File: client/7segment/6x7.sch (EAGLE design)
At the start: 26 parts, among them IC1 AT90S2313P, IC2 7805T

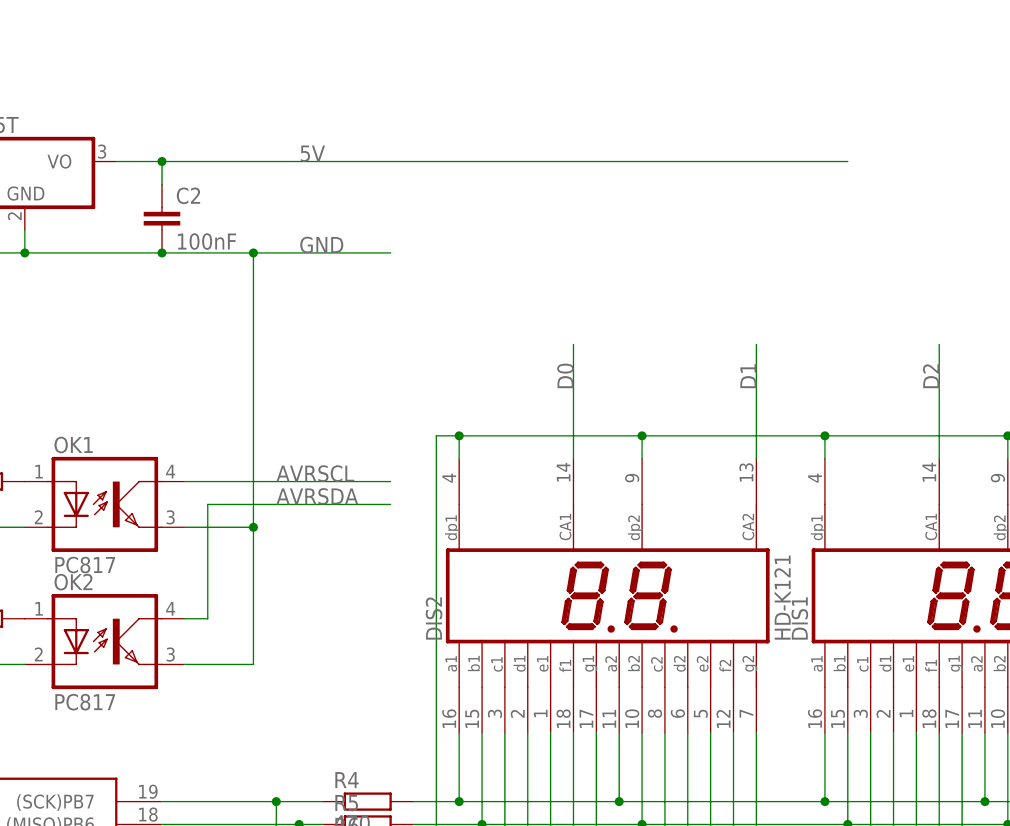
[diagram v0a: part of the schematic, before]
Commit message: 7segment: Add external SDA/SCL pull-ups to allow higher clock rates
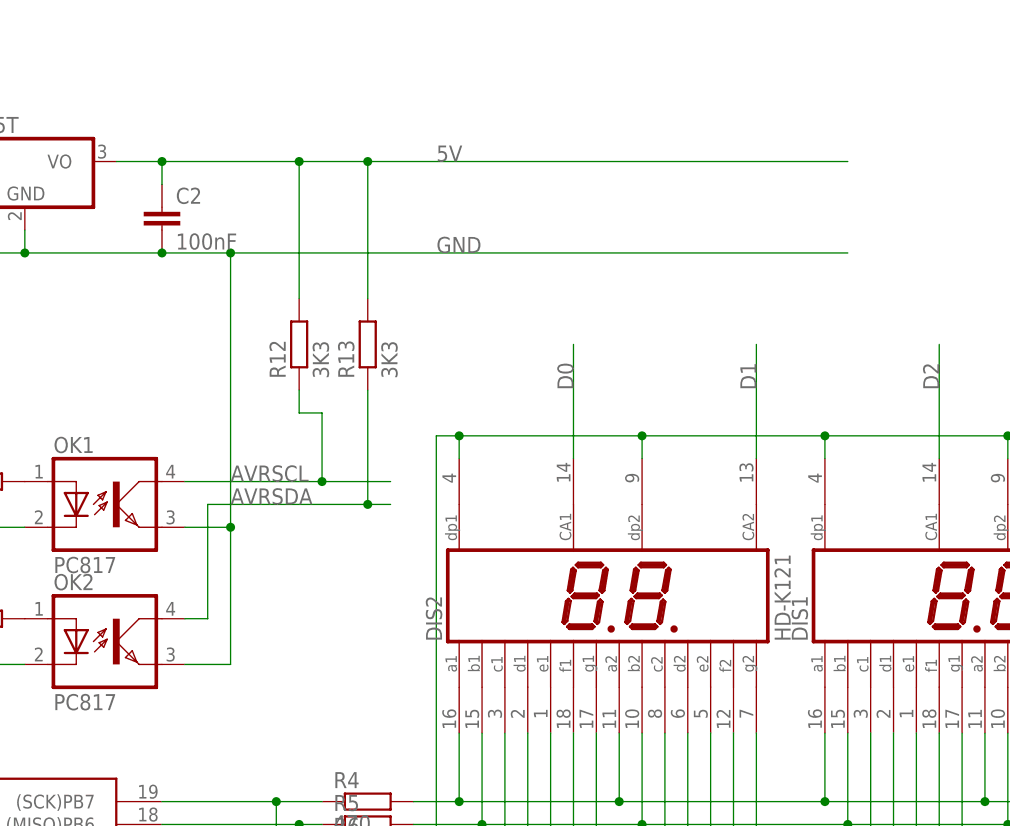
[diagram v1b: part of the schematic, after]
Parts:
- added R12, R13: 3K3, rcl:R-EU_0207/10
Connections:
- net 5V: now also R12.2, R13.2
- net AVRSCL: now also R12.1
- net AVRSDA: now also R13.1
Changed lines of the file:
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@@
 <?xml version="1.0" encoding="utf-8"?>
 <!DOCTYPE eagle SYSTEM "eagle.dtd">
-<eagle version="6.6.0">
+<eagle version="7.5.0">
 <drawing>
 <settings>
@@
 <part name="H3" library="holes" deviceset="MOUNT-HOLE" device="3.2"/>
 <part name="H4" library="holes" deviceset="MOUNT-HOLE" device="3.2"/>
+<part name="R12" library="rcl" deviceset="R-EU_" device="0207/10" value="3K3"/>
+<part name="R13" library="rcl" deviceset="R-EU_" device="0207/10" value="3K3"/>
 </parts>
 <sheets>
@@
 <instance part="H3" gate="G$1" x="-66.04" y="86.36"/>
 <instance part="H4" gate="G$1" x="-66.04" y="78.74"/>
+<instance part="R12" gate="G$1" x="20.32" y="68.58" rot="R90"/>
+<instance part="R13" gate="G$1" x="27.94" y="68.58" rot="R90"/>
 </instances>
 <busses>
@@
 <wire x1="-25.4" y1="78.74" x2="-10.16" y2="78.74" width="0.1524" layer="91"/>
 <wire x1="-10.16" y1="78.74" x2="5.08" y2="78.74" width="0.1524" layer="91"/>
-<wire x1="5.08" y1="78.74" x2="15.24" y2="78.74" width="0.1524" layer="91"/>
+<wire x1="5.08" y1="78.74" x2="12.7" y2="78.74" width="0.1524" layer="91"/>
 <pinref part="OK1" gate="A" pin="EMIT"/>
-<wire x1="15.24" y1="78.74" x2="30.48" y2="78.74" width="0.1524" layer="91"/>
-<wire x1="7.62" y1="48.26" x2="15.24" y2="48.26" width="0.1524" layer="91"/>
-<wire x1="15.24" y1="48.26" x2="15.24" y2="78.74" width="0.1524" layer="91"/>
-<junction x="15.24" y="78.74"/>
+<wire x1="12.7" y1="78.74" x2="81.28" y2="78.74" width="0.1524" layer="91"/>
+<wire x1="7.62" y1="48.26" x2="12.7" y2="48.26" width="0.1524" layer="91"/>
+<wire x1="12.7" y1="48.26" x2="12.7" y2="78.74" width="0.1524" layer="91"/>
+<junction x="12.7" y="78.74"/>
 <junction x="-25.4" y="78.74"/>
-<label x="20.32" y="78.74" size="1.778" layer="95"/>
+<label x="35.56" y="78.74" size="1.778" layer="95"/>
 <junction x="5.08" y="78.74"/>
 <junction x="-10.16" y="78.74"/>
-<wire x1="7.62" y1="33.02" x2="15.24" y2="33.02" width="0.1524" layer="91"/>
+<wire x1="7.62" y1="33.02" x2="12.7" y2="33.02" width="0.1524" layer="91"/>
 <pinref part="OK2" gate="A" pin="EMIT"/>
-<wire x1="15.24" y1="33.02" x2="15.24" y2="48.26" width="0.1524" layer="91"/>
-<junction x="15.24" y="48.26"/>
+<wire x1="12.7" y1="33.02" x2="12.7" y2="48.26" width="0.1524" layer="91"/>
+<junction x="12.7" y="48.26"/>
 </segment>
 </net>
@@
 <segment>
 <pinref part="OK1" gate="A" pin="COL"/>
-<wire x1="7.62" y1="53.34" x2="30.48" y2="53.34" width="0.1524" layer="91"/>
-<label x="17.78" y="53.34" size="1.778" layer="95"/>
+<wire x1="7.62" y1="53.34" x2="22.86" y2="53.34" width="0.1524" layer="91"/>
+<label x="12.7" y="53.34" size="1.778" layer="95"/>
+<pinref part="R12" gate="G$1" pin="1"/>
+<wire x1="22.86" y1="53.34" x2="30.48" y2="53.34" width="0.1524" layer="91"/>
+<wire x1="20.32" y1="63.5" x2="20.32" y2="60.96" width="0.1524" layer="91"/>
+<wire x1="20.32" y1="60.96" x2="22.86" y2="60.96" width="0.1524" layer="91"/>
+<wire x1="22.86" y1="60.96" x2="22.86" y2="53.34" width="0.1524" layer="91"/>
+<junction x="22.86" y="53.34"/>
 </segment>
 <segment>
@@
 <wire x1="5.08" y1="86.36" x2="5.08" y2="88.9" width="0.1524" layer="91"/>
 <junction x="5.08" y="88.9"/>
-<label x="20.32" y="88.9" size="1.778" layer="95"/>
-<wire x1="5.08" y1="88.9" x2="81.28" y2="88.9" width="0.1524" layer="91"/>
+<label x="35.56" y="88.9" size="1.778" layer="95"/>
+<wire x1="5.08" y1="88.9" x2="20.32" y2="88.9" width="0.1524" layer="91"/>
+<pinref part="R12" gate="G$1" pin="2"/>
+<wire x1="20.32" y1="88.9" x2="27.94" y2="88.9" width="0.1524" layer="91"/>
+<wire x1="27.94" y1="88.9" x2="81.28" y2="88.9" width="0.1524" layer="91"/>
+<wire x1="20.32" y1="73.66" x2="20.32" y2="88.9" width="0.1524" layer="91"/>
+<pinref part="R13" gate="G$1" pin="2"/>
+<wire x1="27.94" y1="73.66" x2="27.94" y2="88.9" width="0.1524" layer="91"/>
+<junction x="20.32" y="88.9"/>
+<junction x="27.94" y="88.9"/>
 </segment>
 <segment>
@@
 <wire x1="10.16" y1="38.1" x2="7.62" y2="38.1" width="0.1524" layer="91"/>
 <wire x1="10.16" y1="38.1" x2="10.16" y2="50.8" width="0.1524" layer="91"/>
-<wire x1="10.16" y1="50.8" x2="30.48" y2="50.8" width="0.1524" layer="91"/>
-<label x="17.78" y="50.8" size="1.778" layer="95"/>
-</segment>
-<segment>
+<wire x1="10.16" y1="50.8" x2="27.94" y2="50.8" width="0.1524" layer="91"/>
+<label x="12.7" y="50.8" size="1.778" layer="95"/>
+<pinref part="R13" gate="G$1" pin="1"/>
+<wire x1="27.94" y1="50.8" x2="30.48" y2="50.8" width="0.1524" layer="91"/>
+<wire x1="27.94" y1="63.5" x2="27.94" y2="50.8" width="0.1524" layer="91"/>
+<junction x="27.94" y="50.8"/>
+</segment>
+<segment>
